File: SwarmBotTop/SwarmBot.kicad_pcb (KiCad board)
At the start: 4 copper layers, 50 x 50 mm, 69 parts, among them IC1 ESP32-PICO-D4, IC2 PCA9532BS,118, J1 Conn_01x04_Female, J2 Conn_01x04_Female, J3 Conn_01x04_Female, J4 USB_B_Micro, J5 Conn_01x02_Male, J6 Conn_01x24_Female, Q1 MMBT3904, Q2 MMBT3904, SW1 SW_Push_Open, SW2 SW_Push_Open, U1 CP2102N-A01-GQFN24, U2 MIC5366-3.3YC5, U3 STSPIN220, U4 LIS2DH, U5 MIC5366-3.3YC5, U6 MIC5366-2.8YC5, U7 MIC5366-1.3YC5

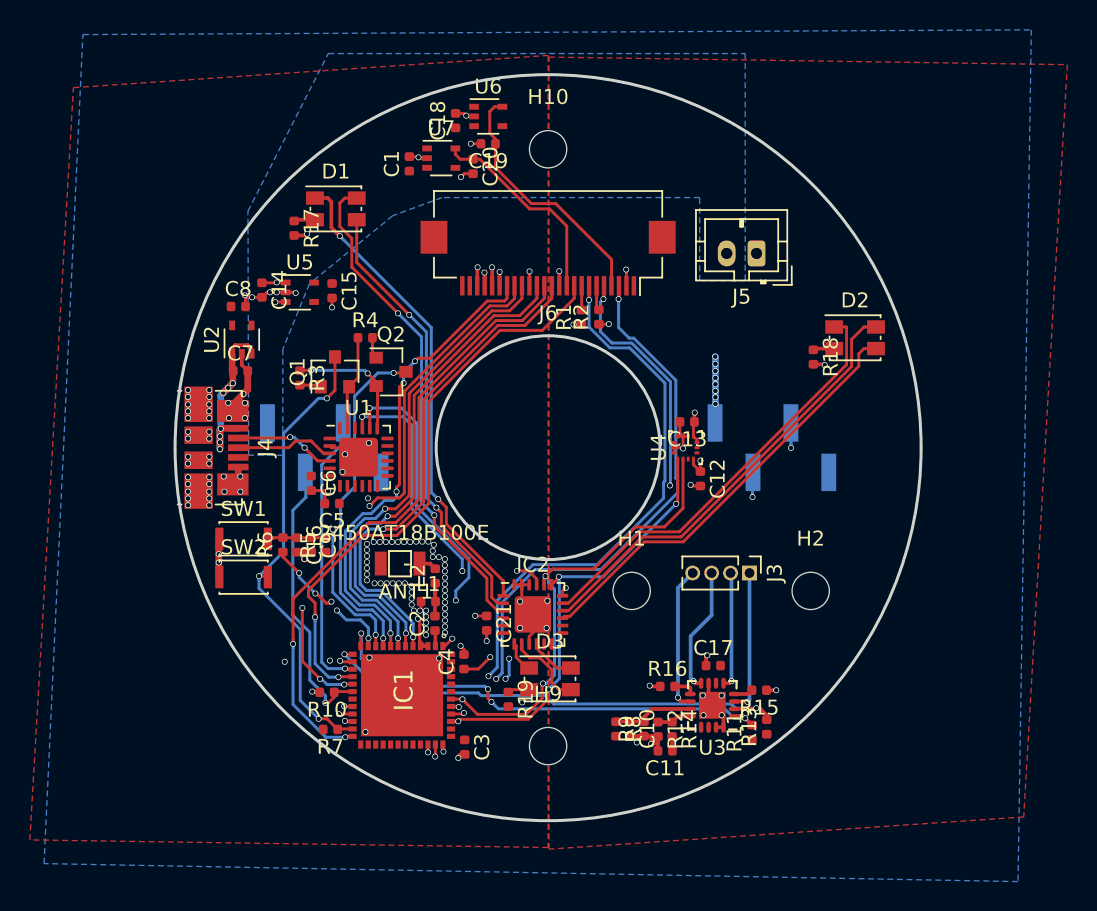
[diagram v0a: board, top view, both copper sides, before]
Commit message: Camera routing with all sensors and motors
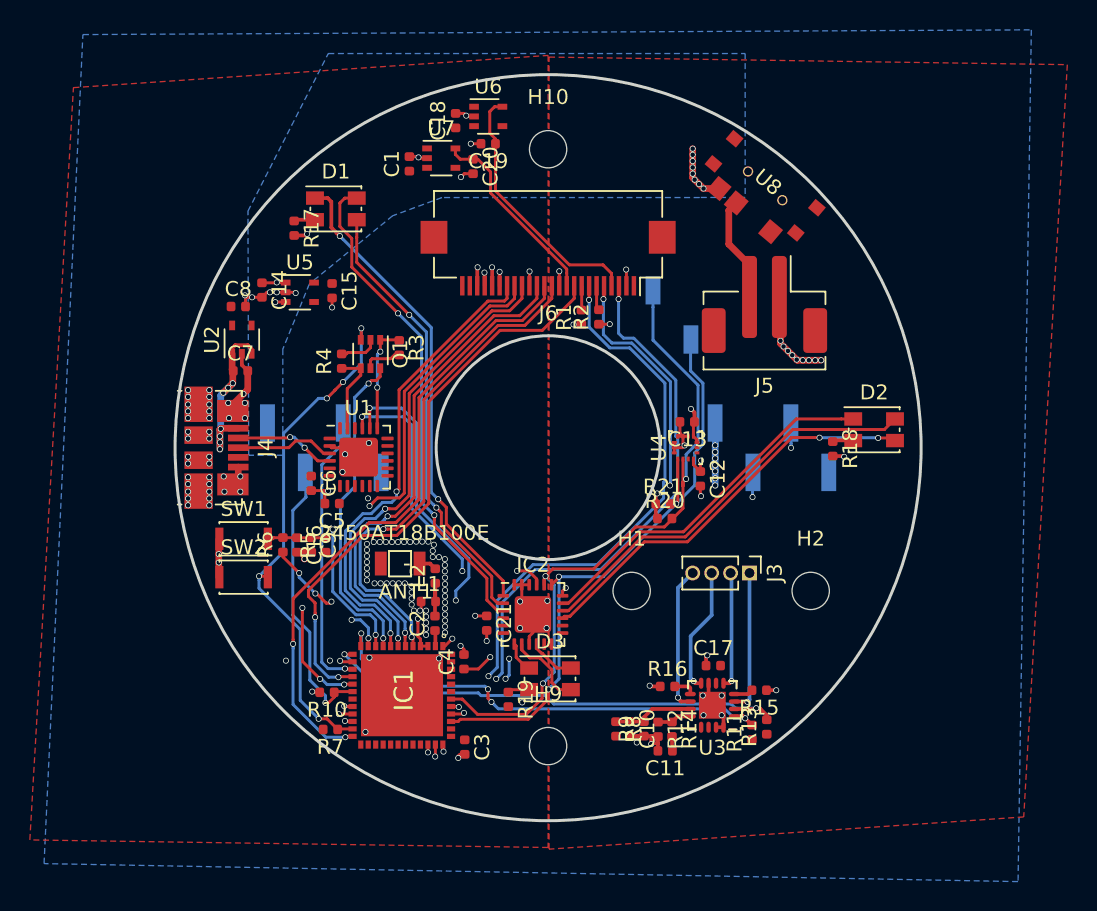
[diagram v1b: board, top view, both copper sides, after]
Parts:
- removed Q2: MMBT3904, Package_TO_SOT_SMD:SOT-23
- added J7: Conn_01x02_Female, Connector_PinSocket_2.54mm:PinSocket_1x02_P2.54mm_Vertical_SMD_Pin1Left, B.Cu at (8.30, -8.90)
- added R20: 10K, Resistor_SMD:R_0402_1005Metric, F.Cu at (7.82, 4.75)
- added R21: 10K, Resistor_SMD:R_0402_1005Metric, F.Cu at (7.70, 3.78)
- added U8: MAX314CSE, switch:K3-1296S-E1, F.Cu at (14.6, -17.6)
- C1, C14, C15, C17, C18, C19, C20, C21, C7, C8: value C -> 1uF
- C10, C12, C13, C16, C4, C6, C9: value C -> 0.1uF
- C11: value C -> 22nF
- C2: value C -> 1.2pF
- C3: value C -> 47uF
- C5: value C -> 4.7uF
- J5: footprint Connector_JST:JST_PH_B2B-PH-K_1x02_P2.00mm_Vertical -> Connector_JST:JST_PH_B2B-PH-SM4-TB_1x02-1MP_P2.00mm_Vertical
- L1: value L -> 2.7nH
- L2: value L -> 3.3nH
- Q1: value MMBT3904 -> MBT3904DW1; footprint Package_TO_SOT_SMD:SOT-23 -> Package_TO_SOT_SMD:SOT-363_SC-70-6
- R1, R10, R11, R13, R2, R3, R4, R5: value R -> 10K
- R12, R7: value R -> 10k
- R14: value R -> 1K
- R15, R16: value R -> 200m
- R17, R18, R19: value R -> 330R
- moved R3 6.96 mm to (-9.98, -6.70)
- moved D2 6.30 mm to (21.9, -1.20)
- moved R18 6.29 mm to (19.1, 0.08)
- moved J5 3.46 mm to (14.5, -9.60)
- moved Q1 2.66 mm to (-11.9, -6.28), turned to 270 degrees
- moved R4 2.23 mm to (-13.8, -5.80), turned to 90 degrees
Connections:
- J5 pad 2: +BATT -> +4V
- Q1 pad 1: Net-(Q1-Pad1) -> /Sheet5DAF9EB0/Programmer/RTS
- Q1 pad 2: /Sheet5DAF9EB0/Programmer/DTR -> Net-(Q1-Pad2)
- R3 pad 2: Net-(Q1-Pad1) -> Net-(Q1-Pad5)
- R4 pad 2: Net-(Q2-Pad1) -> Net-(Q1-Pad2)
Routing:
- net /Sheet5DAF9EB0/SDA: track 30.9 -> 45.5 mm
- net /Sheet5DAF9EB0/SCL: track 29.3 -> 41.8 mm, vias 4 -> 3
- net +4V: track 0.00 -> 7.10 mm
- net GND: track 49.1 -> 55.5 mm, vias 130 -> 139
- net /Sheet5DAF9EB0/LEDS/L3: track 29.0 -> 24.6 mm
- net +BATT: track 6.82 -> 10.5 mm, vias 10 -> 17
- net /Sheet5DAF9EB0/IO0: track 31.5 -> 35.0 mm, vias 3 -> 5
- net Net-(Q1-Pad2): track 0.00 -> 2.63 mm
- net Net-(Q1-Pad5): track 0.00 -> 2.60 mm
- net /Sheet5DAF9EB0/LEDS/L4: track 29.9 -> 27.6 mm
- net +3V3: track 19.5 -> 21.1 mm, vias 15 -> 16
- net /Sheet5DAF9EB0/LEDS/L5: track 29.0 -> 27.4 mm, vias 0 -> 2
- net Net-(Q1-Pad1): track 1.45 -> 0.00 mm
- net Net-(Q2-Pad1): track 1.44 -> 0.00 mm
- net /Sheet5DAF9EB0/EN: track 33.3 -> 32.0 mm
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
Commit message: V1 ready to order
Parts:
- added U9: 62674-241121ALF, ffc:FCI_62674-241121ALF, F.Cu at (-5.73, -15.8)
- C3: value 47uF -> 10uF
- D1, D2, D3: value LED_BGRA -> LED_ARGB; footprint LED_SMD:LED_Kingbright_AAA3528ESGCT -> LED_SMD:LED_SK6812_EC15_1.5x1.5mm
- J5: footprint Connector_JST:JST_PH_B2B-PH-SM4-TB_1x02-1MP_P2.00mm_Vertical -> Connector_PinHeader_1.27mm:PinHeader_1x02_P1.27mm_Horizontal
- J6: value Conn_01x24_Female -> Conn_01x02_Male; footprint Connector_FFC-FPC:Hirose_FH12-24S-0.5SH_1x24-1MP_P0.50mm_Horizontal -> Connector_PinHeader_1.27mm:PinHeader_1x02_P1.27mm_Horizontal
- R6: value R -> 10K
- moved J6 29.3 mm to (22.5, 6.13)
- moved R20 15.0 mm to (9.20, -10.2), turned to 180 degrees
- moved J5 14.3 mm to (5.02, -20.4), turned to 90 degrees
- moved R21 13.1 mm to (9.32, -9.25), turned to 180 degrees
- moved R19 6.60 mm to (3.61, 14.8), turned to 90 degrees
- moved R18 2.51 mm to (21.5, 0.57), turned to 0 degrees
- moved D3 1.70 mm to (1.78, 15.9), turned to 270 degrees
- moved R17 1.63 mm to (-16.1, -16.0)
- moved D2 0.41 mm to (21.4, -1.24), turned to 90 degrees
- moved C12 0.35 mm to (10.0, 1.77), turned to 180 degrees
- moved D1 0.20 mm to (-14.2, -16.2)
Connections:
- D1 pad 1: /Sheet5DAF9EB0/LEDS/L0 -> Net-(D1-Pad1)
- D1 pad 2: /Sheet5DAF9EB0/LEDS/L1 -> /Sheet5DAF9EB0/LEDS/L0
- D1 pad 3: /Sheet5DAF9EB0/LEDS/L2 -> /Sheet5DAF9EB0/LEDS/L1
- D1 pad 4: Net-(D1-Pad4) -> /Sheet5DAF9EB0/LEDS/L2
- D2 pad 1: /Sheet5DAF9EB0/LEDS/L3 -> Net-(D2-Pad1)
- D2 pad 2: /Sheet5DAF9EB0/LEDS/L4 -> /Sheet5DAF9EB0/LEDS/L5
- D2 pad 3: /Sheet5DAF9EB0/LEDS/L5 -> /Sheet5DAF9EB0/LEDS/L4
- D2 pad 4: Net-(D2-Pad4) -> /Sheet5DAF9EB0/LEDS/L3
- D3 pad 1: /Sheet5DAF9EB0/LEDS/L6 -> Net-(D3-Pad1)
- D3 pad 4: Net-(D3-Pad4) -> /Sheet5DAF9EB0/LEDS/L6
- J6 pad 1: (no net) -> GND
- J6 pad 2: GND -> +4V
- R17 pad 1: Net-(D1-Pad4) -> Net-(D1-Pad1)
- R18 pad 1: Net-(D2-Pad4) -> Net-(D2-Pad1)
- R19 pad 1: Net-(D3-Pad4) -> Net-(D3-Pad1)
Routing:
- net +4V: track 7.10 -> 40.2 mm, vias 0 -> 9
- net GND: track 55.5 -> 49.7 mm, vias 139 -> 131
- net /Sheet5DAF9EB0/LEDS/L6: track 2.10 -> 7.95 mm, vias 0 -> 2
- net /Sheet5DAF9EB0/IO5: track 44.8 -> 49.6 mm
- net /Sheet5DAF9EB0/SCL1: track 42.4 -> 47.2 mm
- net /Sheet5DAF9EB0/IO27: track 38.8 -> 43.5 mm, vias 2 -> 4
- net /Sheet5DAF9EB0/IO13: track 36.6 -> 39.7 mm
- net /Sheet5DAF9EB0/SCL: track 41.8 -> 44.9 mm, vias 3 -> 4
- net /Sheet5DAF9EB0/IO34: track 32.6 -> 35.5 mm
- net /Sheet5DAF9EB0/IO4: track 42.0 -> 44.5 mm
- net /Sheet5DAF9EB0/IO25: track 33.2 -> 35.7 mm
- net /Sheet5DAF9EB0/LEDS/L2: track 30.1 -> 32.1 mm
- net /Sheet5DAF9EB0/LEDS/L1: track 33.4 -> 31.3 mm
- net /Sheet5DAF9EB0/SDA1: track 44.9 -> 46.9 mm
- net /Sheet5DAF9EB0/LEDS/L0: track 32.4 -> 30.5 mm
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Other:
- board text added: "Keion Bisland 2019"
- board text added: "SwarmBot V1 TopBoard"

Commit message: things
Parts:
- removed H9: MountingHole, MountingHole:MountingHole_2.5mm
- added H3: MountingHole_Pad, MountingHole:MountingHole_2.5mm_Pad, F.Cu at (0.00, 20.0)
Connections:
- IC1 pad 12: /Sheet5DAF9EB0/PENSTEP -> /Sheet5DAF9EB0/CAPTOUCH
- IC1 pad 38: (no net) -> /Sheet5DAF9EB0/PENSTEP
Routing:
- net /Sheet5DAF9EB0/CAPTOUCH: track 0.00 -> 17.5 mm, vias 0 -> 2
- net /Sheet5DAF9EB0/PENSTEP: track 31.7 -> 22.0 mm, vias 4 -> 2
- net GND: track 49.7 -> 51.7 mm, vias 131 -> 133

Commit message: Final Design
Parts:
- removed J4: USB_B_Micro, Connector_USB:USB_Micro-B_Molex_47346-0001
- removed L1: 2.7nH, Inductor_SMD:L_0402_1005Metric
- removed L2: 3.3nH, Inductor_SMD:L_0402_1005Metric
- removed Q1: MBT3904DW1, Package_TO_SOT_SMD:SOT-363_SC-70-6
- removed SW2: SW_Push_Open, Button_Switch_SMD:SW_SPST_CK_KXT3
- removed U2: MIC5366-3.3YC5, Package_TO_SOT_SMD:SOT-353_SC-70-5
- added C22: 0.1uF, Capacitor_SMD:C_0402_1005Metric, F.Cu at (-18.8, 14.0)
- added C23: 1uF, Capacitor_SMD:C_0402_1005Metric, F.Cu at (-11.0, -12.1)
- added D4: LED, LED_SMD:LED_0603_1608Metric, F.Cu at (15.5, -17.0)
- added D6: LED_ARGB, LED_SMD:LED_SK6812_EC15_1.5x1.5mm, F.Cu at (-22.7, -1.27)
- added D7: LED_ARGB, LED_SMD:LED_SK6812_EC15_1.5x1.5mm, F.Cu at (-13.4, 18.3)
- added D8: LED_ARGB, LED_SMD:LED_SK6812_EC15_1.5x1.5mm, F.Cu at (-16.1, -15.4)
- added R22: 10K, Resistor_SMD:R_0402_1005Metric, F.Cu at (-14.9, 14.0)
- added TP1: TestPoint, TestPoint:TestPoint_Pad_D1.0mm, B.Cu at (-17.4, -6.66)
- added TP2: TestPoint, TestPoint:TestPoint_Pad_D1.0mm, B.Cu at (-14.8, -6.91)
- added TP3: TestPoint, TestPoint:TestPoint_Pad_D1.0mm, B.Cu at (-17.5, -9.11)
- added TP4: TestPoint, TestPoint:TestPoint_Pad_D1.0mm, B.Cu at (-14.8, -9.18)
- added U10: ESP-PSRAM64, Package_SO:SOP-8_3.9x4.9mm_P1.27mm, F.Cu at (-16.9, 10.7)
- added U11: XM25QH32B, Package_SO:SOIC-8_5.275x5.275mm_P1.27mm, F.Cu at (-16.6, 5.06)
- added Y1: 40MHz, Crystal:Crystal_SMD_2520-4Pin_2.5x2.0mm, F.Cu at (-15.2, -2.26)
- C2: value 1.2pF -> 0.1uF
- C3: value 10uF -> 0.1uF
- C5: value 4.7uF -> 3.3nF
- C6: value 0.1uF -> 1uF
- C7: value 1uF -> 12Pf
- C8: value 1uF -> 12pF
- C9: value 0.1uF -> 10nF
- IC1: value ESP32-PICO-D4 -> PCA9532BS,118; footprint ESP32-PICO-D4:ESP32-PICO-D4_1 -> Package_DFN_QFN:VQFN-24-1EP_4x4mm_P0.5mm_EP2.45x2.45mm
- J1, J2: footprint Connector_PinHeader_2.54mm:PinHeader_1x04_P2.54mm_Vertical_SMD_Pin1Left -> Connector_PinHeader_2.54mm:PinHeader_1x04_P2.54mm_Vertical_SMD_Pin1Right
- J5, J6: footprint Connector_PinHeader_1.27mm:PinHeader_1x02_P1.27mm_Horizontal -> Connector_PinHeader_2.54mm:PinHeader_1x02_P2.54mm_Horizontal
- J7: footprint Connector_PinSocket_2.54mm:PinSocket_1x02_P2.54mm_Vertical_SMD_Pin1Left -> Connector_PinSocket_2.54mm:PinSocket_1x02_P2.54mm_Vertical_SMD_Pin1Right
- R10, R4: value 10K -> 330R
- R6: value 10K -> 20K
- R7: value 10k -> 330R
- R8: value R -> 1K
- R9: value R -> 10K
- U1: value CP2102N-A01-GQFN24 -> ESP32-D0WD; footprint Package_DFN_QFN:QFN-24-1EP_4x4mm_P0.5mm_EP2.6x2.6mm -> footprints:ESP32-D0WD
- moved R17 44.2 mm to (5.63, 22.4)
- moved D1 42.7 mm to (4.10, 22.4), turned to 270 degrees
- moved R9 35.4 mm to (16.3, -15.2), turned to 210 degrees
- moved R10 33.4 mm to (-16.0, -17.0), turned to 0 degrees
- moved C14 33.4 mm to (-4.26, 19.3), turned to 90 degrees
- moved U5 31.2 mm to (-6.52, 19.1), turned to 180 degrees
- moved C15 30.3 mm to (-8.67, 19.2), turned to 90 degrees
- moved C2 27.0 mm to (-17.8, -13.3), turned to 0 degrees
- moved D3 26.4 mm to (22.5, -0.44), turned to 0 degrees
- moved C3 26.3 mm to (-12.1, -5.45), turned to 90 degrees
- moved R19 25.3 mm to (22.5, -1.97), turned to 0 degrees
- moved R18 23.2 mm to (10.8, -20.1)
- moved SW1 22.8 mm to (-12.2, -15.1)
- moved C4 21.6 mm to (-19.0, -2.70), turned to 0 degrees
- moved C16 20.5 mm to (-11.0, -13.1), turned to 180 degrees
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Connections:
- C16 pad 1: Net-(C16-Pad1) -> /Sheet5DAF9EB0/EN
- C2 pad 1: Net-(C2-Pad1) -> GND
- C2 pad 2: Net-(C2-Pad2) -> +3V3
- C3 pad 1: +3V3 -> GND
- C3 pad 2: GND -> +3V3
- C4 pad 1: +3V3 -> GND
- C4 pad 2: GND -> +3V3
- C5 pad 1: +3V3 -> Net-(C5-Pad1)
- C5 pad 2: GND -> Net-(C5-Pad2)
- C7 pad 1: +5V -> GND
- C7 pad 2: GND -> Net-(C7-Pad2)
- C8 pad 1: +3V3 -> GND
- C8 pad 2: GND -> Net-(C8-Pad2)
- C9 pad 1: Net-(C16-Pad1) -> GND
- C9 pad 2: GND -> Net-(C5-Pad1)
- IC1 pad 1: +3V3 -> (no net)
- IC1 pad 10: /Sheet5DAF9EB0/IO34 -> /Sheet5DAF9EB0/LEDS/L17
- IC1 pad 11: /Sheet5DAF9EB0/IO35 -> /Sheet5DAF9EB0/LEDS/L9
- IC1 pad 12: /Sheet5DAF9EB0/CAPTOUCH -> /Sheet5DAF9EB0/LEDS/L10
- IC1 pad 13: /Sheet5DAF9EB0/PENDIR -> /Sheet5DAF9EB0/LEDS/L11
- IC1 pad 14: /Sheet5DAF9EB0/IO25 -> (no net)
- IC1 pad 15: /Sheet5DAF9EB0/RMOTDIR -> /Sheet5DAF9EB0/LEDS/L14
- IC1 pad 16: /Sheet5DAF9EB0/IO27 -> /Sheet5DAF9EB0/LEDS/L13
- IC1 pad 17: /Sheet5DAF9EB0/IO14 -> /Sheet5DAF9EB0/LEDS/L12
- IC1 pad 18: /Sheet5DAF9EB0/RMOTSTEP -> +3V3
- IC1 pad 19: +3V3 -> /Sheet5DAF9EB0/SCL
- IC1 pad 2: Net-(C2-Pad1) -> (no net)
- IC1 pad 20: /Sheet5DAF9EB0/IO13 -> /Sheet5DAF9EB0/SDA
- IC1 pad 21: /Sheet5DAF9EB0/LMOTSTEP -> +3V3
- IC1 pad 22: /Sheet5DAF9EB0/LMOTDIR -> GND
- IC1 pad 23: /Sheet5DAF9EB0/IO0 -> +3V3
- IC1 pad 24: /Sheet5DAF9EB0/IO4 -> GND
- IC1 pad 25: (no net) -> GND
- IC1 pad 3: +3V3 -> (no net)
- IC1 pad 4: +3V3 -> (no net)
- IC1 pad 5: /Sheet5DAF9EB0/S_VP -> (no net)
- IC1 pad 6: /Sheet5DAF9EB0/IO37 -> (no net)
- IC1 pad 7: /Sheet5DAF9EB0/IO38 -> /Sheet5DAF9EB0/LEDS/L15
- IC1 pad 8: /Sheet5DAF9EB0/S_VN -> /Sheet5DAF9EB0/LEDS/L16
- IC1 pad 9: /Sheet5DAF9EB0/EN -> GND
- IC2 pad 1: /Sheet5DAF9EB0/LEDS/L0 -> (no net)
- IC2 pad 10: /Sheet5DAF9EB0/LEDS/L7 -> /Sheet5DAF9EB0/PENSTEP
- IC2 pad 11: (no net) -> /Sheet5DAF9EB0/PENDIR
- IC2 pad 12: (no net) -> /Sheet5DAF9EB0/LEDS/L6
- IC2 pad 13: (no net) -> /Sheet5DAF9EB0/LEDS/L8
- IC2 pad 14: (no net) -> /Sheet5DAF9EB0/LEDS/L7
- IC2 pad 15: /Sheet5DAF9EB0/LEDS/L5 -> /Sheet5DAF9EB0/LEDS/L3
- IC2 pad 17: /Sheet5DAF9EB0/LEDS/L3 -> /Sheet5DAF9EB0/LEDS/L5
- IC2 pad 2: /Sheet5DAF9EB0/LEDS/L2 -> (no net)
- IC2 pad 3: /Sheet5DAF9EB0/LEDS/L1 -> (no net)
- IC2 pad 4: (no net) -> /Sheet5DAF9EB0/LEDS/L0
- IC2 pad 5: (no net) -> /Sheet5DAF9EB0/LEDS/L1
- IC2 pad 6: (no net) -> /Sheet5DAF9EB0/LEDS/L2
- IC2 pad 7: /Sheet5DAF9EB0/LEDS/L6 -> /Sheet5DAF9EB0/CURRSET
- IC2 pad 8: /Sheet5DAF9EB0/LEDS/L8 -> /Sheet5DAF9EB0/STEPPEREN
- R10 pad 1: /Sheet5DAF9EB0/RMOTSTEP -> Net-(D8-Pad1)
- R10 pad 2: GND -> +3V3
- R11 pad 1: +BATT -> +3V3
- R13 pad 1: +BATT -> +3V3
- R3 pad 1: /Sheet5DAF9EB0/Programmer/RTS -> Net-(R3-Pad1)
- R3 pad 2: Net-(Q1-Pad5) -> +3V3
- R4 pad 1: /Sheet5DAF9EB0/Programmer/DTR -> Net-(D6-Pad1)
- R4 pad 2: Net-(Q1-Pad2) -> +3V3
- R5 pad 2: Net-(C16-Pad1) -> /Sheet5DAF9EB0/EN
- R6 pad 1: /Sheet5DAF9EB0/EN -> Net-(C5-Pad1)
- R6 pad 2: Net-(C16-Pad1) -> Net-(C5-Pad2)
- R7 pad 1: /Sheet5DAF9EB0/IO0 -> Net-(D7-Pad1)
- R8 pad 2: +BATT -> /Sheet5DAF9EB0/CURRSET
- R9 pad 1: GND -> Net-(D4-Pad2)
- R9 pad 2: Net-(C10-Pad1) -> +BATT
- SW1 pad 2: Net-(C16-Pad1) -> /Sheet5DAF9EB0/EN
- U1 pad 1: (no net) -> +3V3
- U1 pad 10: (no net) -> /Sheet5DAF9EB0/IO34
- U1 pad 11: (no net) -> /Sheet5DAF9EB0/IO35
- U1 pad 12: (no net) -> /Sheet5DAF9EB0/CAPTOUCH
- U1 pad 13: (no net) -> /Sheet5DAF9EB0/RMOTDIR
- U1 pad 14: (no net) -> /Sheet5DAF9EB0/IO25
- U1 pad 15: (no net) -> /Sheet5DAF9EB0/RMOTSTEP
- U1 pad 16: (no net) -> /Sheet5DAF9EB0/IO27
- U1 pad 17: (no net) -> /Sheet5DAF9EB0/IO14
- U1 pad 18: (no net) -> Net-(R3-Pad1)
- U1 pad 19: /Sheet5DAF9EB0/Programmer/RTS -> +3V3
- U1 pad 2: GND -> Net-(ANT1-Pad1)
- U1 pad 20: /Sheet5DAF9EB0/TX -> /Sheet5DAF9EB0/IO13
- U1 pad 21: /Sheet5DAF9EB0/RX -> /Sheet5DAF9EB0/LMOTSTEP
- U1 pad 22: (no net) -> /Sheet5DAF9EB0/LMOTDIR
- U1 pad 23: /Sheet5DAF9EB0/Programmer/DTR -> /Sheet5DAF9EB0/IO0
- U1 pad 24: (no net) -> /Sheet5DAF9EB0/IO4
- U1 pad 25: GND -> /Sheet5DAF9EB0/IO16
- U1 pad 3: /Sheet5DAF9EB0/Programmer/D_P -> +3V3
- U1 pad 4: /Sheet5DAF9EB0/Programmer/D_N -> +3V3
- U1 pad 5: +3V3 -> /Sheet5DAF9EB0/S_VP
- U1 pad 6: +3V3 -> /Sheet5DAF9EB0/IO37
- U1 pad 7: +3V3 -> /Sheet5DAF9EB0/IO38
- U1 pad 8: +3V3 -> /Sheet5DAF9EB0/S_VN
- U1 pad 9: (no net) -> /Sheet5DAF9EB0/EN
- U3 pad 13: +BATT -> /Sheet5DAF9EB0/STEPPEREN
- U9 pad 18: /Sheet5DAF9EB0/IO5 -> (no net)
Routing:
- net /Sheet5DAF9EB0/IO5: track 49.6 -> 0.00 mm, vias 3 -> 0
- net /Sheet5DAF9EB0/LEDS/L15: track 0.00 -> 46.7 mm, vias 0 -> 2
- net /Sheet5DAF9EB0/LEDS/L16: track 0.00 -> 45.1 mm, vias 0 -> 2
- net /Sheet5DAF9EB0/LEDS/L17: track 0.00 -> 43.9 mm, vias 0 -> 2
- net /Sheet5DAF9EB0/IO0: track 35.0 -> 2.69 mm, vias 5 -> 1
- net /Sheet5DAF9EB0/LEDS/L9: track 0.00 -> 27.5 mm, vias 0 -> 2
- net VDD_SDIO: track 0.00 -> 27.2 mm, vias 0 -> 3
- net /Sheet5DAF9EB0/IO17: track 0.00 -> 26.2 mm, vias 0 -> 3
- net /Sheet5DAF9EB0/SD3: track 0.00 -> 25.9 mm, vias 0 -> 2
- net /Sheet5DAF9EB0/LEDS/L10: track 0.00 -> 25.6 mm, vias 0 -> 2
- net /Sheet5DAF9EB0/TX: track 27.7 -> 3.19 mm, vias 3 -> 1
- net /Sheet5DAF9EB0/LEDS/L11: track 0.00 -> 24.2 mm, vias 0 -> 2
- net /Sheet5DAF9EB0/IO13: track 39.7 -> 15.6 mm
- net /Sheet5DAF9EB0/CMD: track 0.00 -> 24.1 mm, vias 0 -> 3
- net /Sheet5DAF9EB0/SD0: track 0.00 -> 24.0 mm, vias 0 -> 3
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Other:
- rule trace_min: 0.175 -> 0.125
- rule via_min_drill: 0.3 -> 0.2
- rule via_min_size: 0.4 -> 0.3
- board text added: "+"
- board text added: "-"
- board text added: "Keion Bisland 2020"
- board text added: "SwarmBot V2 TopBoard"
- board text removed: "Keion Bisland 2019"
- board text removed: "SwarmBot V1 TopBoard"

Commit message: Updated LED drivers
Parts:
- IC1, IC2: value PCA9532BS,118 -> MAX7313ATG+; footprint Package_DFN_QFN:VQFN-24-1EP_4x4mm_P0.5mm_EP2.45x2.45mm -> MAX7313ATG+:QFN50P400X400X80-25N
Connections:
- IC1 pad 22: GND -> (no net)
- IC2 pad 22: GND -> (no net)
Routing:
- net GND: track 54.8 -> 54.2 mm, vias 63 -> 62
